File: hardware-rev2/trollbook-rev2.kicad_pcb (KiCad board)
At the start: 4 copper layers, 100 x 100 mm, 35 parts, among them CON1 FPGA JTAG, CON2 CPU JTAG, P4 ER-CON40HT-1, Q1 2N7002E, Q2 2N7002E, U1 MC68040FC33V, U10 ADA4851-4, U2 EPF10K50VRC240, U3 EPC2, U4 HY57V561620, U5 HY57V561620, U6 AS7C34098, U7 74LVC138, U8 MCP4902, U9 S25FL204K0TMFI010

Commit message: almost done
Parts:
- added P1: /BR, Measurement_Points:Measurement_Point_Square-SMD-Pad_Small, F.Cu at (180.8, 138.5)
- added P2: /CDIS, Resistors_SMD:R_0805, B.Cu at (151.5, 139.8)
- added P3: Audio, Pin_Headers:Pin_Header_Straight_1x04, F.Cu at (87.5, 122.6)
- added P5: Power, Pin_Headers:Pin_Header_Straight_1x04, F.Cu at (87.5, 136.5)
- added P6: Peripheral, Pin_Headers:Pin_Header_Straight_1x16, F.Cu at (87.5, 106.1)
- added P7: VGA, Pin_Headers:Pin_Header_Straight_1x06, F.Cu at (151.7, 52.9)
- added P8: Clocks, Pin_Headers:Pin_Header_Straight_1x04, F.Cu at (87.5, 61.5)
- added Q3: DMP3030SN-7, Housings_SOT-23_SOT-143_TSOT-6:SOT-23_Handsoldering, B.Cu at (102.7, 81.5)
- added R1: R, Resistors_SMD:R_0805_HandSoldering, F.Cu at (149.5, 147.1)
- added R10: R, Resistors_SMD:R_0805_HandSoldering, F.Cu at (154.3, 147.1)
- added R11: R, Resistors_SMD:R_0805_HandSoldering, F.Cu at (146.2, 147.1)
- added R12: 10k, Resistors_SMD:R_0805_HandSoldering, B.Cu at (95.2, 81.8)
- added R13: 470k, Resistors_SMD:R_0805_HandSoldering, B.Cu at (91.5, 89.7)
- added R14: 20R, Resistors_SMD:R_0805_HandSoldering, B.Cu at (97.1, 92.4)
- added R15: R, Resistors_SMD:R_0805_HandSoldering, B.Cu at (98.0, 81.8)
- added R2: 10k, Resistors_SMD:R_0805_HandSoldering, F.Cu at (166.6, 147.1)
- added R28: 1k, Resistors_SMD:R_0805_HandSoldering, F.Cu at (90.5, 93.8)
- added R29: R, Resistors_SMD:R_0805_HandSoldering, F.Cu at (158.7, 147.1)
- added R3: 10k, Resistors_SMD:R_0805_HandSoldering, F.Cu at (168.9, 147.1)
- added R4: 10k, Resistors_SMD:R_0805_HandSoldering, F.Cu at (171.2, 147.1)
- added R5: 10k, Resistors_SMD:R_0805_HandSoldering, F.Cu at (182.2, 140.5)
- added R6: 10k, Resistors_SMD:R_0805_HandSoldering, F.Cu at (152.0, 147.1)
- added R7: 1k, Resistors_SMD:R_0805_HandSoldering, F.Cu at (104.5, 131.1)
- added R8: 1k, Resistors_SMD:R_0805_HandSoldering, F.Cu at (105.9, 134.8)
- added R9: 1k, Resistors_SMD:R_0805_HandSoldering, F.Cu at (98.3, 139.5)
- added RP10: R_PACK4, mod:RPACK8_SMD, F.Cu at (130.4, 138.7)
- added RP9: R_PACK4, mod:RPACK8_SMD, F.Cu at (105.0, 138.4)
- added U11: 33 MHz, trollbook:OSC-VCC1-B3B, F.Cu at (179.2, 83.5)
- added U12: 12.288 MHz, trollbook:OSC-ASFLMB, F.Cu at (92.0, 63.5)
- Q1, Q2: moved to B.Cu
- moved Q2 76.7 mm to (96.9, 86.4), turned to 90 degrees
- moved Q1 76.3 mm to (96.9, 89.7), turned to 270 degrees
- moved CON1 42.9 mm to (108.6, 143.8), turned to 270 degrees
- moved CON2 24.0 mm to (135.2, 143.8), turned to 270 degrees
- moved U8 7.98 mm to (93.2, 102.0)
- moved U3 6.83 mm to (97.9, 132.8)
- moved U7 5.31 mm to (95.7, 73.1)
- moved U9 5.29 mm to (95.8, 82.5)
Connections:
- CON1 pad 1: (no net) -> /FPGA_TCK
- CON1 pad 10: (no net) -> GND
- CON1 pad 2: (no net) -> GND
- CON1 pad 3: (no net) -> /CONF_TDO
- CON1 pad 5: (no net) -> /FPGA_TMS
- CON1 pad 9: (no net) -> /FPGA_TDI
- CON2 pad 1: (no net) -> /CPUTCK
- CON2 pad 10: (no net) -> GND
- CON2 pad 2: (no net) -> GND
- CON2 pad 3: (no net) -> /CPUTDO
- CON2 pad 5: (no net) -> /CPUTMS
- CON2 pad 9: (no net) -> /CPUTDI
- P4 pad 13: (no net) -> GND
- P4 pad 14: (no net) -> GND
- P4 pad 2: (no net) -> /VGALED_ANODE
- P4 pad 21: (no net) -> GND
- P4 pad 22: (no net) -> GND
- P4 pad 23: (no net) -> GND
- P4 pad 31: (no net) -> /VGADISP
- P4 pad 32: /VGAHSYNC -> /VGADISP
- P4 pad 33: /VGAVSYNC -> /VGADISP
- P4 pad 34: (no net) -> /VGADEN
- P4 pad 36: (no net) -> GND
- P4 pad 4: (no net) -> /VGADISP
- P4 pad 5: (no net) -> GND
- P4 pad 6: (no net) -> GND
- P4 pad 7: (no net) -> GND
- Q1 pad 2: (no net) -> GND
- R25 pad 1: (no net) -> Net-(P7-Pad1)
- R26 pad 1: (no net) -> Net-(P7-Pad2)
- R27 pad 1: (no net) -> Net-(P7-Pad3)
- U1 pad 11: (no net) -> /CPUCDIS
- U1 pad 18: /CLK33 -> /CPUCLK
- U1 pad 2: (no net) -> /CPUTDO
- U1 pad 26: (no net) -> Net-(R29-Pad2)
- U1 pad 3: (no net) -> /CPUTDI
- U1 pad 34: (no net) -> /CPUSC0
- U1 pad 35: (no net) -> /CPUSC1
- U1 pad 36: (no net) -> /CPUBG
- U1 pad 4: (no net) -> /CPUTCK
- U1 pad 47: (no net) -> /CPUBB
- U1 pad 50: (no net) -> /CPUBR
- U1 pad 6: (no net) -> /CPULOC
- U1 pad 7: (no net) -> /CPUTMS
- U2 pad 1: (no net) -> /FPGA_TCK
- U2 pad 127: /RAMCLK -> /VGADEN
- U2 pad 177: (no net) -> /FPGA_TDI
- U2 pad 181: (no net) -> /VGALED_PWM
- U2 pad 184: /VGAR2 -> /VGAR0
- U2 pad 188: /SPI0MOSI -> /SPI0CLK
- U2 pad 190: /SPI0CLK -> /SPI0MOSI
- U2 pad 191: /VGAR0 -> /VGAR2
- U2 pad 209: (no net) -> /PWRON_RESET
- U2 pad 211: (no net) -> /CLK12
- U2 pad 23: (no net) -> /VGAPWR
- U2 pad 239: (no net) -> /UARTTX
- U2 pad 240: (no net) -> /UARTRX
- U2 pad 26: (no net) -> /CPUCLK
- U2 pad 4: (no net) -> /FPGA_TDO
- U2 pad 58: (no net) -> /FPGA_TMS
- U3 pad 12: (no net) -> GND
- U3 pad 13: (no net) -> /FPGA_TDO
- U3 pad 25: (no net) -> /FPGA_TMS
- U3 pad 28: (no net) -> /CONF_TDO
- U3 pad 32: (no net) -> /FPGA_TCK
- U4 pad 38: /RAMCLK -> /CLK33
- U5 pad 38: /RAMCLK -> /CLK33
- U7 pad 10: (no net) -> /SPI0SS5
- U7 pad 11: (no net) -> /SPI0SS4
- U7 pad 12: (no net) -> /SPI0SS3
- U7 pad 13: (no net) -> /SPI0SS2
- U7 pad 16: (no net) -> +3V3
- U7 pad 7: (no net) -> /SPI0SS7
- U7 pad 9: (no net) -> /SPI0SS6
- U8 pad 10: (no net) -> Net-(P3-Pad1)
- U8 pad 14: (no net) -> Net-(P3-Pad4)
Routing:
- net GND: track 27.5 -> 267.4 mm, vias 12 -> 91
- net +3V3: track 12.9 -> 243.4 mm, vias 6 -> 81
- net /FPGA_TDI: track 0.00 -> 108.2 mm, vias 0 -> 2
- net /CONF_CLK: track 0.00 -> 98.8 mm, vias 0 -> 2
- net /CONF_DATA: track 0.00 -> 95.7 mm, vias 0 -> 2
- net /CLK33: track 63.9 -> 145.5 mm, vias 2 -> 5
- net /CONF_INIT: track 0.00 -> 77.4 mm, vias 0 -> 2
- net /FPGA_TMS: track 0.00 -> 74.3 mm, vias 0 -> 2
- net /CONF_OE: track 0.00 -> 73.1 mm, vias 0 -> 2
- net /CPUCLK: track 0.00 -> 68.6 mm, vias 0 -> 2
- net /FPGA_TCK: track 0.00 -> 63.7 mm, vias 0 -> 3
- net /VGALED_ANODE: track 0.00 -> 52.2 mm, vias 0 -> 1
- net /VGAPWR: track 0.00 -> 41.0 mm, vias 0 -> 1
- net /CLK12: track 0.00 -> 40.2 mm, vias 0 -> 2
- net /CONF_CS: track 0.00 -> 38.0 mm, vias 0 -> 2
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
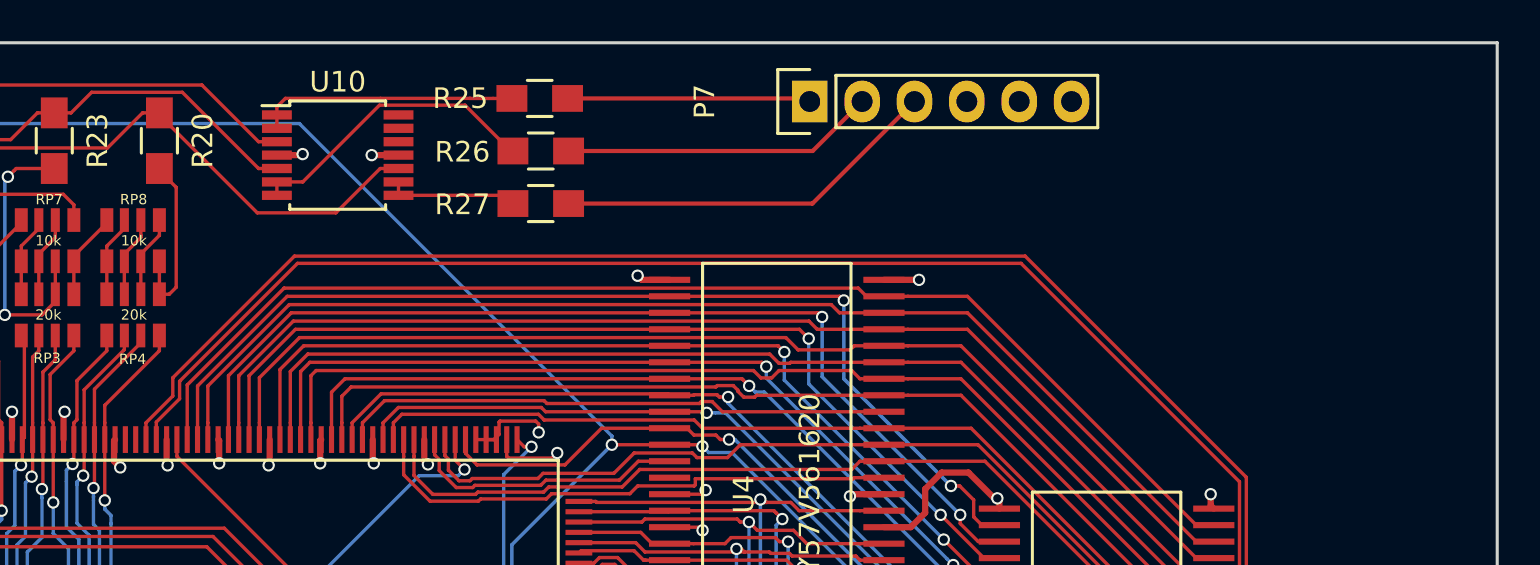
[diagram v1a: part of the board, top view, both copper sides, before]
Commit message: now only the capacitors left
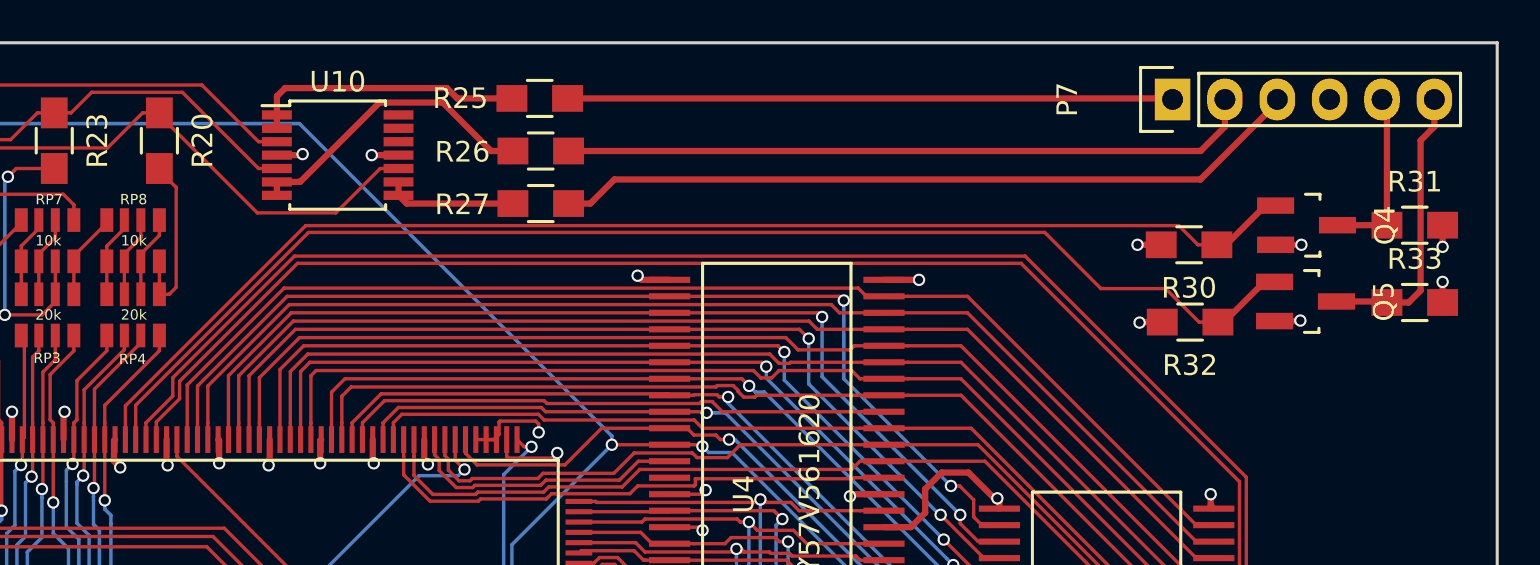
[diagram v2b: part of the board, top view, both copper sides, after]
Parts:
- added Q4: 2N7002E, Housings_SOT-23_SOT-143_TSOT-6:SOT-23_Handsoldering, F.Cu at (175.8, 58.9)
- added Q5: 2N7002E, Housings_SOT-23_SOT-143_TSOT-6:SOT-23_Handsoldering, F.Cu at (175.7, 62.5)
- added R30: R, Resistors_SMD:R_0805_HandSoldering, F.Cu at (170.1, 59.8)
- added R31: R, Resistors_SMD:R_0805_HandSoldering, F.Cu at (181.0, 58.9)
- added R32: R, Resistors_SMD:R_0805_HandSoldering, F.Cu at (170.1, 63.5)
- added R33: R, Resistors_SMD:R_0805_HandSoldering, F.Cu at (181.0, 62.6)
- moved P7 17.6 mm to (169.2, 52.8)
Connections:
- P7 pad 5: /VGAHSYNC -> Net-(P7-Pad5)
- P7 pad 6: /VGAVSYNC -> Net-(P7-Pad6)
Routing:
- net /VGAVSYNC: track 0.00 -> 63.0 mm
- net /VGAHSYNC: track 0.00 -> 62.2 mm
- net Net-(P7-Pad2): track 15.2 -> 33.6 mm
- net Net-(P7-Pad3): track 18.8 -> 36.6 mm
- net Net-(P7-Pad1): track 11.8 -> 29.4 mm
- net Net-(P7-Pad6): track 0.00 -> 13.9 mm
- net Net-(P7-Pad5): track 0.00 -> 8.60 mm
- net +3V3: track 243.4 -> 250.8 mm, vias 81 -> 85
- net GND: track 267.4 -> 271.1 mm, vias 91 -> 93
- net Net-(R25-Pad2): track 12.6 -> 13.3 mm
- net Net-(R27-Pad2): track 6.37 -> 6.93 mm

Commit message: capacitors, capacitors everywhere
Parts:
- added C1: 220u, Capacitors_SMD:c_elec_6.3x7.7, F.Cu at (90.1, 143.9)
- added C10: 100n, Capacitors_SMD:C_0805_HandSoldering, B.Cu at (145.4, 72.8)
- added C11: 100n, Capacitors_SMD:C_0805_HandSoldering, B.Cu at (158.4, 76.5)
- added C12: 100n, Capacitors_SMD:C_0805_HandSoldering, B.Cu at (172.5, 73.0)
- added C13: 100n, Capacitors_SMD:C_0805_HandSoldering, B.Cu at (165.8, 82.2)
- added C14: 100n, Capacitors_SMD:C_0805_HandSoldering, B.Cu at (172.8, 94.3)
- added C15: 100n, Capacitors_SMD:C_0805_HandSoldering, B.Cu at (160.6, 87.9)
- added C16: 100n, Capacitors_SMD:C_0805_HandSoldering, B.Cu at (118.5, 124.2)
- added C17: 100n, Capacitors_SMD:C_0805_HandSoldering, B.Cu at (110.3, 123.5)
- added C18: 100n, Capacitors_SMD:C_0805_HandSoldering, B.Cu at (124.2, 69.2)
- added C19: 100n, Capacitors_SMD:C_0805_HandSoldering, B.Cu at (135.8, 67.3)
- added C2: 10u, Capacitors_SMD:C_1206_HandSoldering, F.Cu at (90.2, 129.4)
- added C20: 100n, Capacitors_SMD:C_0805_HandSoldering, F.Cu at (102.3, 82.0)
- added C21: 100n, Capacitors_SMD:C_0805_HandSoldering, B.Cu at (110.7, 69.2)
- added C22: 100n, Capacitors_SMD:C_0805_HandSoldering, B.Cu at (104.9, 95.7)
- added C23: 100n, Capacitors_SMD:C_0805_HandSoldering, B.Cu at (140.4, 78.2)
- added C24: 100n, Capacitors_SMD:C_0805_HandSoldering, B.Cu at (140.5, 85.0)
- added C25: 100n, Capacitors_SMD:C_0805_HandSoldering, B.Cu at (116.7, 69.2)
- added C26: 100n, Capacitors_SMD:C_0805_HandSoldering, B.Cu at (112.4, 107.8)
- added C27: 100n, Capacitors_SMD:C_0805_HandSoldering, B.Cu at (115.2, 105.0)
- added C28: 100n, Capacitors_SMD:C_0805_HandSoldering, B.Cu at (104.9, 78.1)
- added C29: 100n, Capacitors_SMD:C_0805_HandSoldering, B.Cu at (140.5, 89.7)
- added C3: 100n, Capacitors_SMD:C_0805_HandSoldering, B.Cu at (94.0, 134.4)
- added C30: 100n, Capacitors_SMD:C_0805_HandSoldering, B.Cu at (140.5, 95.5)
- added C31: 100n, Capacitors_SMD:C_0805_HandSoldering, B.Cu at (129.2, 69.3)
- added C32: 100n, Capacitors_SMD:C_0805_HandSoldering, B.Cu at (119.2, 102.3)
- added C33: 100n, Capacitors_SMD:C_0805_HandSoldering, B.Cu at (133.9, 69.3)
- added C34: 100n, Capacitors_SMD:C_0805_HandSoldering, B.Cu at (124.7, 109.0)
- added C35: 100n, Capacitors_SMD:C_0805_HandSoldering, B.Cu at (137.7, 98.7)
- added C36: 100n, Capacitors_SMD:C_0805_HandSoldering, B.Cu at (129.8, 110.8)
- added C37: 10n, Capacitors_SMD:C_0805_HandSoldering, B.Cu at (147.5, 107.5)
- added C38: 10n, Capacitors_SMD:C_0805_HandSoldering, B.Cu at (143.2, 139.7)
- added C39: 10n, Capacitors_SMD:C_0805_HandSoldering, B.Cu at (154.8, 102.5)
- added C4: 100n, Capacitors_SMD:C_0805_HandSoldering, B.Cu at (94.0, 97.7)
- added C40: 10n, Capacitors_SMD:C_0805_HandSoldering, F.Cu at (143.8, 106.8)
- added C41: 10n, Capacitors_SMD:C_0805_HandSoldering, B.Cu at (149.2, 109.2)
- added C42: 10n, Capacitors_SMD:C_0805_HandSoldering, B.Cu at (142.2, 135.6)
- added C43: 10n, Capacitors_SMD:C_0805_HandSoldering, B.Cu at (179.8, 119.3)
- added C44: 10n, Capacitors_SMD:C_0805_HandSoldering, B.Cu at (145.8, 128.8)
- added C45: 10n, Capacitors_SMD:C_0805_HandSoldering, B.Cu at (142.2, 119.4)
- added C46: 10n, Capacitors_SMD:C_0805_HandSoldering, B.Cu at (157.8, 105.3)
- added C47: 10n, Capacitors_SMD:C_0805_HandSoldering, B.Cu at (160.2, 107.0)
- added C48: 10n, Capacitors_SMD:C_0805_HandSoldering, B.Cu at (164.1, 108.2)
- added C49: 10n, Capacitors_SMD:C_0805_HandSoldering, B.Cu at (145.8, 126.5)
- added C5: 100n, Capacitors_SMD:C_0805_HandSoldering, B.Cu at (125.8, 56.9)
- added C50: 10n, Capacitors_SMD:C_0805_HandSoldering, B.Cu at (174.9, 142.4)
- added C51: 10n, Capacitors_SMD:C_0805_HandSoldering, B.Cu at (161.8, 142.9)
- added C52: 10n, Capacitors_SMD:C_0805_HandSoldering, B.Cu at (145.8, 122.7)
- added C53: 10n, Capacitors_SMD:C_0805_HandSoldering, B.Cu at (149.8, 143.4)
- added C54: 10n, Capacitors_SMD:C_0805_HandSoldering, B.Cu at (179.8, 123.2)
- added C55: 10n, Capacitors_SMD:C_0805_HandSoldering, B.Cu at (169.0, 142.8)
- added C56: 10n, Capacitors_SMD:C_0805_HandSoldering, B.Cu at (168.6, 107.8)
- added C57: 10n, Capacitors_SMD:C_0805_HandSoldering, B.Cu at (177.8, 138.1)
- added C58: 10n, Capacitors_SMD:C_0805_HandSoldering, B.Cu at (178.1, 129.9)
- added C59: 10n, Capacitors_SMD:C_0805_HandSoldering, B.Cu at (172.1, 107.8)
- added C6: 100n, Capacitors_SMD:C_0805_HandSoldering, B.Cu at (93.0, 75.3)
- added C60: 10n, Capacitors_SMD:C_0805_HandSoldering, B.Cu at (158.4, 139.7)
- added C61: 10n, Capacitors_SMD:C_0805_HandSoldering, B.Cu at (179.1, 125.8)
- added C62: 10n, Capacitors_SMD:C_0805_HandSoldering, B.Cu at (179.1, 116.8)
- added C63: 10n, Capacitors_SMD:C_0805_HandSoldering, B.Cu at (177.8, 112.5)
- added C64: 10n, Capacitors_SMD:C_0805_HandSoldering, B.Cu at (157.2, 143.6)
- added C65: 10n, Capacitors_SMD:C_0805_HandSoldering, B.Cu at (179.1, 134.2)
- added C66: 10n, Capacitors_SMD:C_0805_HandSoldering, B.Cu at (175.3, 109.3)
- added C67: 100n, Capacitors_SMD:C_0805_HandSoldering, B.Cu at (151.1, 111.0)
- added C68: 100n, Capacitors_SMD:C_0805_HandSoldering, B.Cu at (175.2, 135.9)
- added C69: 100n, Capacitors_SMD:C_0805_HandSoldering, B.Cu at (161.8, 144.9)
- added C7: 100n, Capacitors_SMD:C_0805_HandSoldering, B.Cu at (98.2, 76.8)
- added C70: 100n, Capacitors_SMD:C_0805_HandSoldering, B.Cu at (175.3, 114.0)
- added C71: 100n, Capacitors_SMD:C_0805_HandSoldering, B.Cu at (141.1, 139.7)
- added C8: 100n, Capacitors_SMD:C_0805_HandSoldering, B.Cu at (157.0, 61.5)
- added C9: 100n, Capacitors_SMD:C_0805_HandSoldering, B.Cu at (156.8, 82.3)
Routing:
- net GND: track 271.1 -> 404.7 mm, vias 93 -> 108
- net +3V3: track 250.8 -> 376.5 mm, vias 85 -> 87
- net /VGALED_ANODE: track 52.2 -> 55.4 mm
- net /RAMA12: track 36.6 -> 37.9 mm
- net /RAMCKE: track 33.0 -> 34.2 mm
- net /CLK33: track 145.5 -> 146.5 mm
- net /D0: track 49.3 -> 48.7 mm

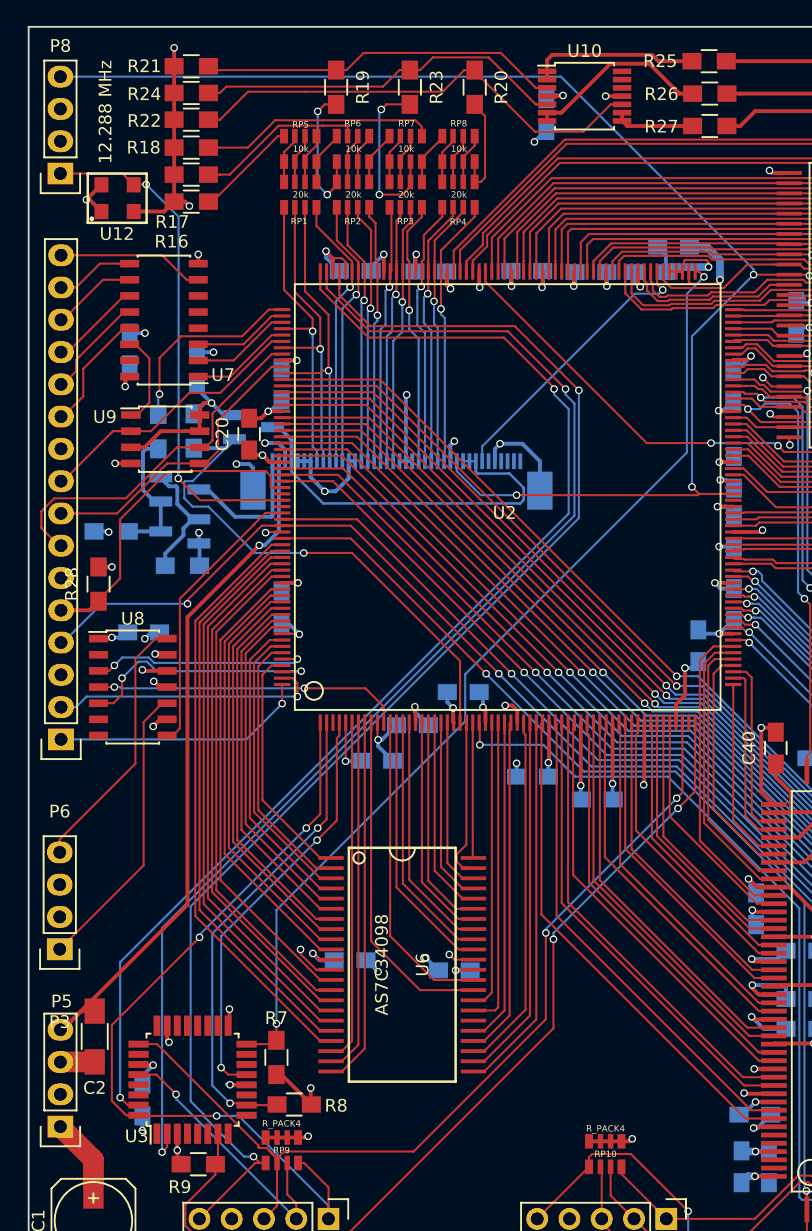
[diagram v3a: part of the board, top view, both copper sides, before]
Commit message: added external interrupt header
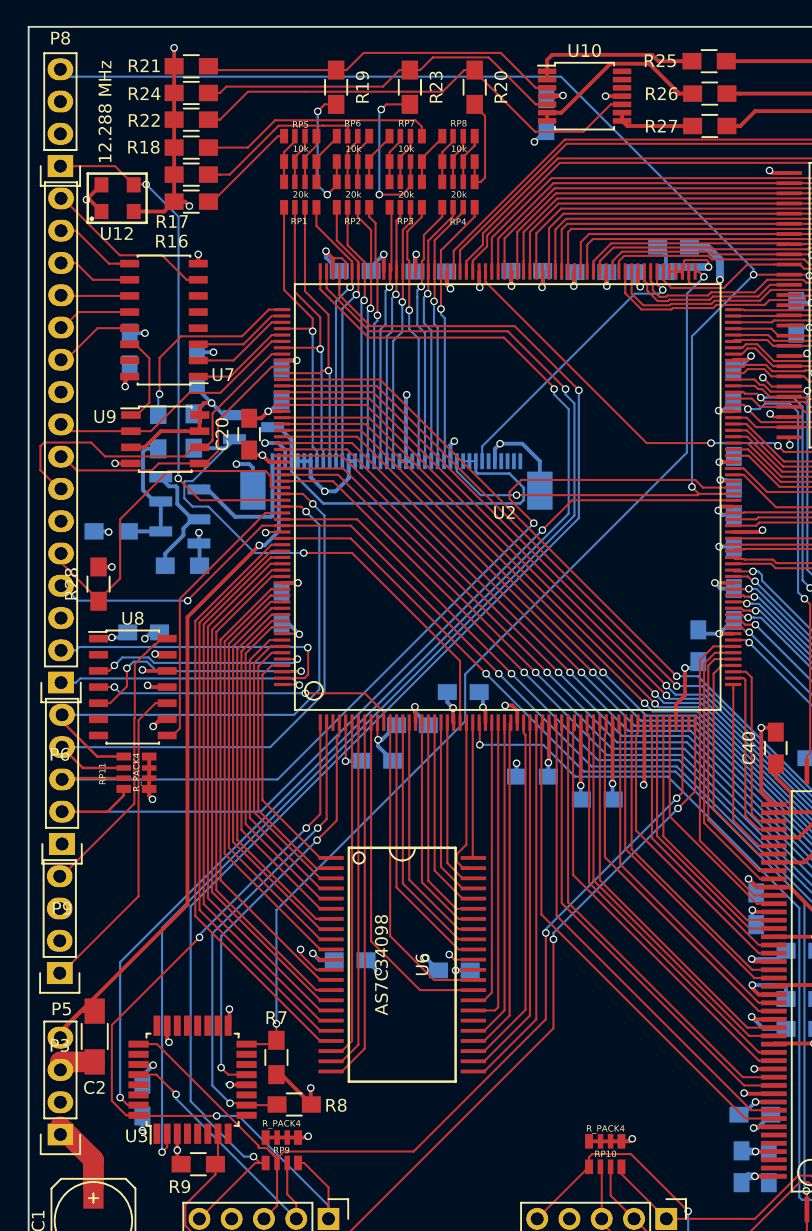
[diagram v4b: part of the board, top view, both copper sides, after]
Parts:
- added P9: CONN_01X05, Pin_Headers:Pin_Header_Straight_1x05, F.Cu at (87.6, 114.3)
- added RP11: R_PACK4, mod:RPACK8_SMD, F.Cu at (93.5, 108.7)
- moved P6 4.47 mm to (87.5, 101.6)
- moved P3 1.88 mm to (87.5, 124.5)
- moved P5 0.62 mm to (87.5, 137.2)
- moved P8 0.58 mm to (87.5, 61.0)
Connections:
- net Net-(P3-Pad1) renamed /AUDIOR
- net Net-(P3-Pad4) renamed /AUDIOL
- U2 pad 210: (no net) -> /EXTINT2
- U2 pad 212: (no net) -> /EXTINT3
- U2 pad 90: (no net) -> /EXTINT0
- U2 pad 92: (no net) -> /EXTINT1
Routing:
- net /EXTINT1: track 0.00 -> 71.9 mm, vias 0 -> 1
- net /EXTINT0: track 0.00 -> 68.9 mm, vias 0 -> 1
- net /EXTINT2: track 0.00 -> 46.0 mm, vias 0 -> 1
- net /EXTINT3: track 0.00 -> 44.1 mm, vias 0 -> 1
- net +3V3: track 376.5 -> 379.7 mm, vias 87 -> 88
- net /UARTTX: track 21.4 -> 24.0 mm
- net /AUDIOR: track 23.4 -> 25.7 mm
- net /SPI0SS2: track 9.55 -> 7.41 mm
- net /SPI0SS7: track 11.6 -> 13.5 mm
- net /PWRON_RESET: track 25.7 -> 27.5 mm
- net /SPI0SS3: track 8.28 -> 6.51 mm
- net /SPI0SS4: track 7.23 -> 5.87 mm
- net GND: track 404.7 -> 406.1 mm
- net /SPI0MISO: track 22.0 -> 20.7 mm
- net /CPURSTI: track 105.4 -> 104.4 mm
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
